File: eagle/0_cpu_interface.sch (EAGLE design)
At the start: 66 parts, among them IC1 74LS08N, IC10 74LS74N, IC11 74LS73N, IC12 MAX1232CPA, IC13 74LS32N, IC14 74LS244N, IC15 74LS74N, IC16 74LS14N, IC17 74LS541N, IC18 74LS541N, IC19 74LS541N, IC2 74LS541N, IC3 74LS245N, IC4 74LS245N, IC6 74LS541N, IC9 74LS74N

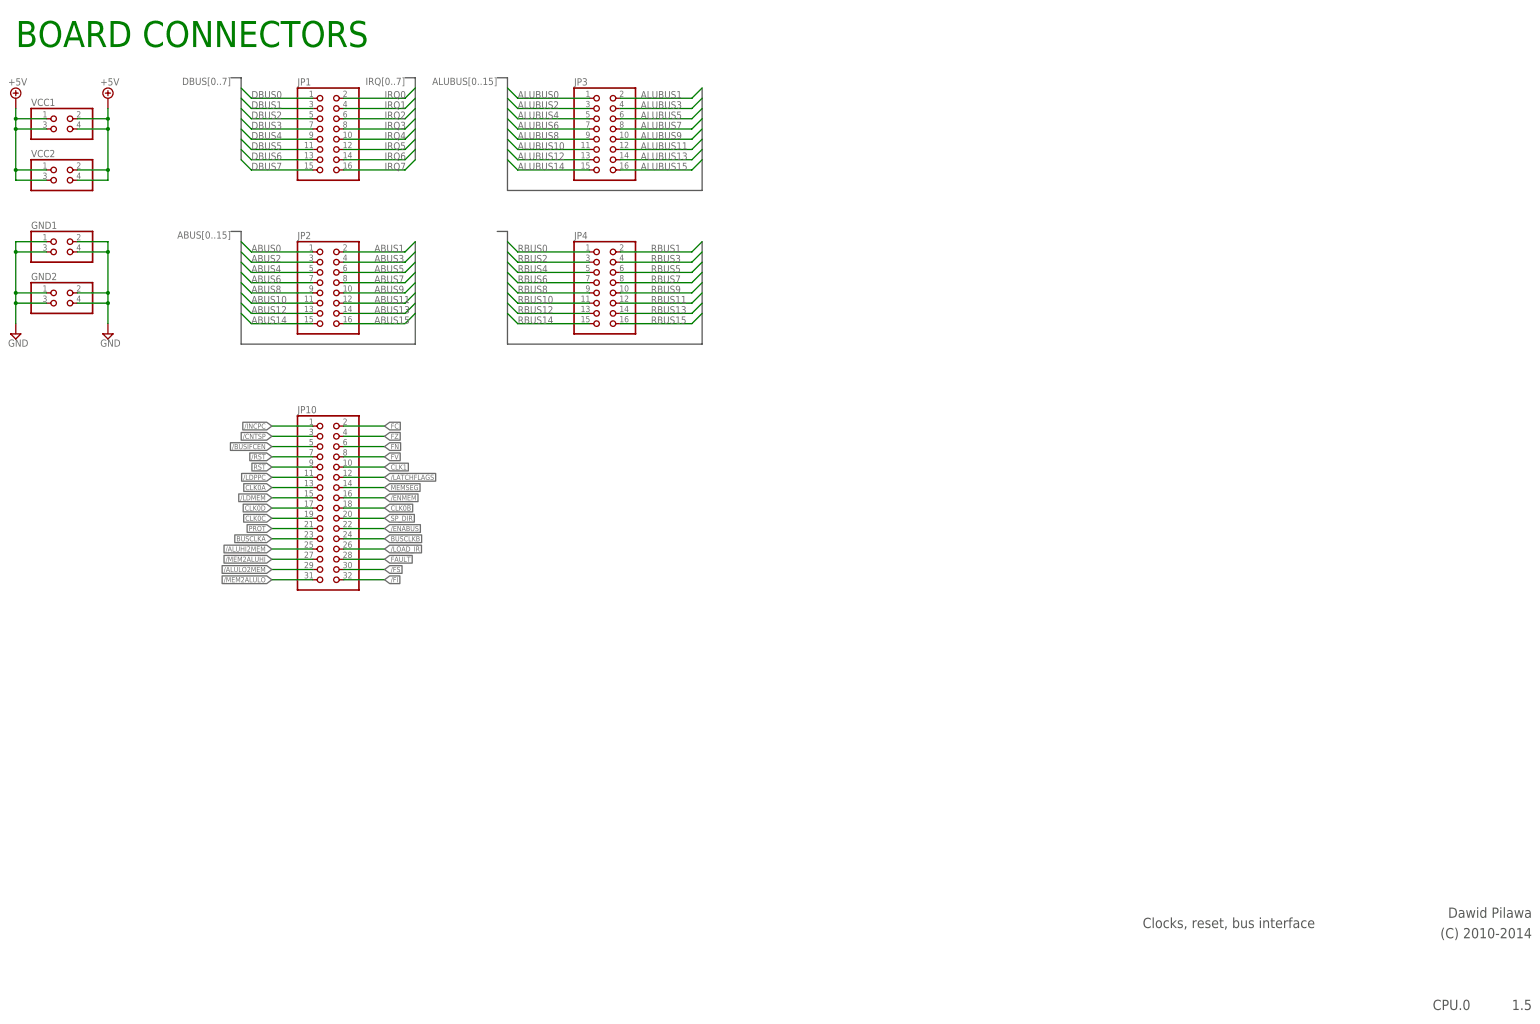
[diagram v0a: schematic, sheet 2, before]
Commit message: All boards prepared for MMU extension
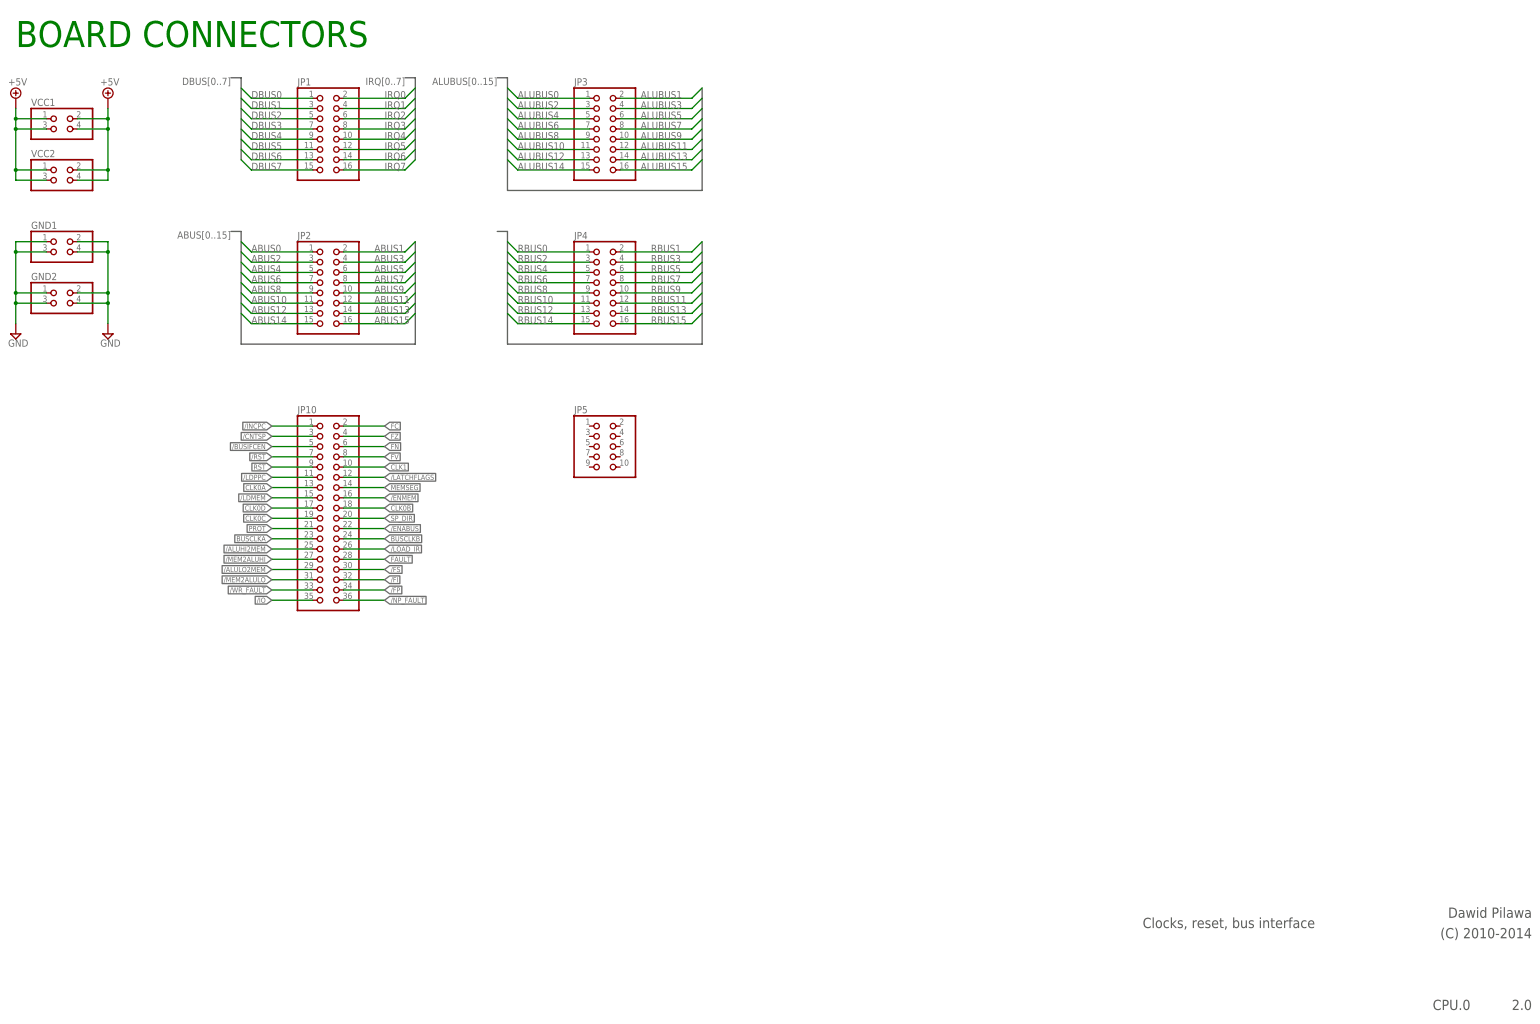
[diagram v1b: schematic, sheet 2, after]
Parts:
- added JP5: (no value), pinhead:PINHD-2X5
- added X1: (no value), con-wago-500:W237-102
- JP10: device pinhead:PINHD-2X16 -> pinhead:PINHD-2X18
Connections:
- new net /FP: JP10.34
- new net /NP_FAULT: JP10.36
- new net /WR_FAULT: JP10.33
- net +5V: now also X1-1.KL
- net /IO: now also JP10.35
- net GND: now also X1-2.KL
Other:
- note added: "2.0"
- note removed: "1.5"
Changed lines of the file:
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@@
 <part name="JP3" library="pinhead" deviceset="PINHD-2X8" device=""/>
 <part name="JP4" library="pinhead" deviceset="PINHD-2X8" device=""/>
-<part name="JP10" library="pinhead" deviceset="PINHD-2X16" device=""/>
+<part name="JP10" library="pinhead" deviceset="PINHD-2X18" device=""/>
 <part name="IC17" library="74xx-eu" deviceset="74*541" device="N" technology="LS"/>
 <part name="IC18" library="74xx-eu" deviceset="74*541" device="N" technology="LS"/>
@@
 <part name="C18" library="rcl" deviceset="CPOL-EU" device="E2.5-6" value="10u"/>
 <part name="FRAME2" library="frames" deviceset="DINA3_L" device=""/>
+<part name="X1" library="con-wago-500" deviceset="W237-102" device=""/>
+<part name="SUPPLY25" library="supply2" deviceset="+5V" device=""/>
+<part name="SUPPLY33" library="supply2" deviceset="GND" device=""/>
+<part name="JP5" library="pinhead" deviceset="PINHD-2X5" device=""/>
 </parts>
 <sheets>
@@
 <text x="386.08" y="27.94" size="2.54" layer="97" font="vector" rot="R180">(C) 2010-2014</text>
 <text x="370.84" y="10.16" size="2.54" layer="97" font="vector" rot="R180">CPU.0</text>
-<text x="386.08" y="10.16" size="2.54" layer="97" font="vector" rot="R180">1.5</text>
+<text x="386.08" y="10.16" size="2.54" layer="97" font="vector" rot="R180">2.0</text>
 <text x="200.16" y="105.56" size="1.778" layer="97" font="vector">/RST is active for ~250ms</text>
 <text x="233.68" y="127" size="1.778" layer="91">CLK0</text>
@@
 <instance part="IC19" gate="P" x="350.52" y="50.8"/>
 <instance part="C18" gate="G$1" x="381" y="81.28"/>
+<instance part="X1" gate="-1" x="205.74" y="93.98"/>
+<instance part="X1" gate="-2" x="205.74" y="88.9"/>
+<instance part="SUPPLY25" gate="+5V" x="215.9" y="93.98" rot="R270"/>
+<instance part="SUPPLY33" gate="GND" x="213.36" y="83.82"/>
 </instances>
 <busses>
@@
 <junction x="147.32" y="22.86"/>
 </segment>
+<segment>
+<pinref part="X1" gate="-1" pin="KL"/>
+<pinref part="SUPPLY25" gate="+5V" pin="+5V"/>
+<wire x1="210.82" y1="93.98" x2="213.36" y2="93.98" width="0.1524" layer="91"/>
+</segment>
 </net>
 <net name="N$3" class="0">
@@
 <junction x="172.72" y="109.22"/>
 </segment>
+<segment>
+<pinref part="X1" gate="-2" pin="KL"/>
+<wire x1="210.82" y1="88.9" x2="213.36" y2="88.9" width="0.1524" layer="91"/>
+<wire x1="213.36" y1="88.9" x2="213.36" y2="86.36" width="0.1524" layer="91"/>
+<pinref part="SUPPLY33" gate="GND" pin="GND"/>
+</segment>
 </net>
 <net name="N$11" class="0">
@@
 <pinref part="J1" gate="G$1" pin="C11"/>
 <wire x1="170.18" y1="83.82" x2="187.96" y2="83.82" width="0.1524" layer="91"/>
-<label x="193.04" y="83.82" size="1.4224" layer="95" rot="R180" xref="yes"/>
+<label x="187.96" y="83.82" size="1.4224" layer="95" xref="yes"/>
 </segment>
 </net>
@@
 <text x="386.08" y="27.94" size="2.54" layer="97" font="vector" rot="R180">(C) 2010-2014</text>
 <text x="370.84" y="10.16" size="2.54" layer="97" font="vector" rot="R180">CPU.0</text>
-<text x="386.08" y="10.16" size="2.54" layer="97" font="vector" rot="R180">1.5</text>
+<text x="386.08" y="10.16" size="2.54" layer="97" font="vector" rot="R180">2.0</text>
 <text x="10.16" y="246.38" size="6.4516" layer="91">BOARD CONNECTORS</text>
 </plain>
@@
 <instance part="JP3" gate="A" x="154.94" y="226.06"/>
 <instance part="JP4" gate="A" x="154.94" y="187.96"/>
-<instance part="JP10" gate="A" x="86.36" y="134.62"/>
+<instance part="JP10" gate="A" x="86.36" y="132.08"/>
+<instance part="JP5" gate="A" x="154.94" y="147.32"/>
 </instances>
 <busses>
@@
 </segment>
 </net>
+<net name="/WR_FAULT" class="0">
+<segment>
+<pinref part="JP10" gate="A" pin="33"/>
+<wire x1="83.82" y1="111.76" x2="73.66" y2="111.76" width="0.1524" layer="91"/>
+<label x="73.66" y="111.76" size="1.27" layer="95" rot="R180" xref="yes"/>
+</segment>
+</net>
+<net name="/FP" class="0">
+<segment>
+<pinref part="JP10" gate="A" pin="34"/>
+<wire x1="91.44" y1="111.76" x2="101.6" y2="111.76" width="0.1524" layer="91"/>
+<label x="101.6" y="111.76" size="1.27" layer="95" xref="yes"/>
+</segment>
+</net>
+<net name="/NP_FAULT" class="0">
+<segment>
+<pinref part="JP10" gate="A" pin="36"/>
+<wire x1="91.44" y1="109.22" x2="101.6" y2="109.22" width="0.1524" layer="91"/>
+<label x="101.6" y="109.22" size="1.27" layer="95" xref="yes"/>
+</segment>
+</net>
+<net name="/IO" class="0">
+<segment>
+<pinref part="JP10" gate="A" pin="35"/>
+<wire x1="83.82" y1="109.22" x2="73.66" y2="109.22" width="0.1524" layer="91"/>
+<label x="73.66" y="109.22" size="1.27" layer="95" rot="R180" xref="yes"/>
+</segment>
+</net>
